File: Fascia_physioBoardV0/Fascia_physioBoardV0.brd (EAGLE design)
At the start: 32.8 x 41.6 mm, 81 parts, among them CN2 CA0612KRX7R9BB102, CN3 CA0612KRX7R9BB102, CN4 CA0612KRX7R9BB102, CN5 CA0612KRX7R9BB102, CN6 CA0612KRX7R9BB102, J1 MOLEX_52437-2471MOLEX_52437-2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, J2 MOLEX_52435-2271MOLEX_52435-2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, U1 ADS1299-X, U10 TPD4E1B06DCKR, U11 TPD4E1B06DCKR, U12 OPA320AIDBVRDBV5-L, U2 OPA2320AIDGKT_NOVA8-SOIC-L, U3 OPA2320AIDGKT_NOVAL8-SOIC-L, U4 HCNR200-300E, U5 OPA320AIDBVRDBV5-L, U6 TPD4E1B06DCKR, U7 TPD4E1B06DCKR, U8 TPD4E1B06DCKR, U9 TPD4E1B06DCKR

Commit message: minor updates
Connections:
- net ADS_CLK: now also J2.1
- net ADS_RESET2: now also J2.5
- net DVDD: now also J2.16, J2.17
- net DVDD_ISO: now also J2.20, J2.21
- net GND: now also J2.12, J2.13, J2.8, J2.9
- net GND_ISO: now also J2.18, J2.19
- net PA07_DRDY2: now also J2.2
- net PA16_S1_MOSI: now also J2.4
- net PA17_S1_SCK: now also J2.6
- net PA19_S1_MISO: now also J2.7
- net PA20_CS2: now also J2.3
- net S0_I2C_SCL: now also J2.11
- net S0_I2C_SDA: now also J2.10
- net VCC: now also J2.14, J2.15
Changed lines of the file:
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@@
 <drawing>
 <settings>
-<setting alwaysvectorfont="yes"/>
+<setting alwaysvectorfont="no"/>
 <setting verticaltext="up"/>
 </settings>
@@
 <signal name="PA19_S1_MISO">
 <contactref element="U1" pad="43"/>
+<contactref element="J2" pad="7"/>
+<wire x1="14.58" y1="29.838" x2="17.15" y2="37.138" width="0" layer="19" extent="1-1"/>
 </signal>
 <signal name="PA17_S1_SCK">
 <contactref element="U1" pad="40"/>
+<contactref element="J2" pad="6"/>
+<wire x1="16.08" y1="29.838" x2="17.65" y2="37.138" width="0" layer="19" extent="1-1"/>
 </signal>
 <signal name="N$66">
@@
 </polygon>
 <contactref element="U5" pad="5"/>
+<contactref element="J2" pad="16"/>
+<contactref element="J2" pad="17"/>
 <wire x1="18.58" y1="29.838" x2="24.05" y2="35.4332" width="0" layer="19" extent="1-16"/>
 <wire x1="12.08" y1="29.838" x2="18.58" y2="29.838" width="0" layer="19" extent="1-1"/>
@@
 <wire x1="8.342" y1="32.712" x2="12.08" y2="29.838" width="0" layer="19" extent="1-1"/>
 <wire x1="6.842" y1="32.712" x2="8.342" y2="32.712" width="0" layer="19" extent="1-1"/>
+<wire x1="12.15" y1="37.138" x2="8.342" y2="32.712" width="0" layer="19" extent="1-1"/>
+<wire x1="12.65" y1="37.138" x2="12.15" y2="37.138" width="0" layer="19" extent="1-1"/>
 </signal>
 <signal name="N$63">
@@
 <signal name="PA16_S1_MOSI">
 <contactref element="U1" pad="34"/>
+<contactref element="J2" pad="4"/>
+<wire x1="19.08" y1="29.838" x2="18.65" y2="37.138" width="0" layer="19" extent="1-1"/>
 </signal>
 <signal name="N$22">
@@
 <contactref element="U4" pad="5"/>
 <contactref element="U5" pad="3"/>
+<contactref element="J2" pad="8"/>
+<contactref element="J2" pad="9"/>
+<contactref element="J2" pad="12"/>
+<contactref element="J2" pad="13"/>
 <wire x1="25.95" y1="37.5668" x2="27.6" y2="37.8" width="0" layer="19" extent="16-16"/>
 <wire x1="25" y1="37.5668" x2="25.95" y2="37.5668" width="0" layer="19" extent="16-16"/>
 <wire x1="21.525" y1="41.01" x2="25" y2="37.5668" width="0" layer="19" extent="16-16"/>
-<wire x1="13.965" y1="40.3" x2="21.525" y2="41.01" width="0" layer="19" extent="1-16"/>
-<wire x1="16.008" y1="33.615" x2="21.525" y2="41.01" width="0" layer="19" extent="1-16"/>
+<wire x1="16.65" y1="37.138" x2="21.525" y2="41.01" width="0" layer="19" extent="1-16"/>
+<wire x1="16.15" y1="37.138" x2="16.65" y2="37.138" width="0" layer="19" extent="1-1"/>
+<wire x1="14.65" y1="37.138" x2="16.15" y2="37.138" width="0" layer="19" extent="1-1"/>
+<wire x1="14.15" y1="37.138" x2="14.65" y2="37.138" width="0" layer="19" extent="1-1"/>
+<wire x1="13.965" y1="40.3" x2="14.15" y2="37.138" width="0" layer="19" extent="1-1"/>
+<wire x1="16.008" y1="33.615" x2="16.15" y2="37.138" width="0" layer="19" extent="1-1"/>
 <wire x1="14.4515" y1="33.215" x2="16.008" y2="33.615" width="0" layer="19" extent="1-1"/>
 <wire x1="13.129" y1="33.215" x2="14.4515" y2="33.215" width="0" layer="19" extent="1-1"/>
@@
 <contactref element="U4" pad="4"/>
 <contactref element="U12" pad="2"/>
+<contactref element="J2" pad="18"/>
+<contactref element="J2" pad="19"/>
 <wire x1="27.191" y1="30.15" x2="25.85" y2="29.9" width="0" layer="19" extent="16-16"/>
-<wire x1="27.9" y1="23" x2="25.85" y2="29.9" width="0" layer="19" extent="16-16"/>
-<wire x1="25.65" y1="23" x2="27.9" y2="23" width="0" layer="19" extent="16-16"/>
+<wire x1="25.65" y1="23" x2="25.85" y2="29.9" width="0" layer="19" extent="16-16"/>
+<wire x1="27.9" y1="23" x2="25.65" y2="23" width="0" layer="19" extent="16-16"/>
 <wire x1="23.013" y1="23.495" x2="25.65" y2="23" width="0" layer="19" extent="16-16"/>
 <wire x1="16.05" y1="29.65" x2="23.013" y2="23.495" width="0" layer="19" extent="16-16"/>
@@
 <wire x1="5" y1="33.1332" x2="5.173" y2="30.831" width="0" layer="19" extent="16-16"/>
 <wire x1="4.05" y1="33.1332" x2="5" y2="33.1332" width="0" layer="19" extent="16-16"/>
+<wire x1="11.15" y1="37.138" x2="5" y2="33.1332" width="0" layer="19" extent="1-16"/>
+<wire x1="11.65" y1="37.138" x2="11.15" y2="37.138" width="0" layer="19" extent="1-1"/>
+<wire x1="10.275" y1="41.01" x2="11.15" y2="37.138" width="0" layer="19" extent="1-16"/>
 <wire x1="1.3" y1="21.1" x2="9.113" y2="23.195" width="0" layer="19" extent="16-16"/>
-<wire x1="10.275" y1="41.01" x2="5" y2="33.1332" width="0" layer="19" extent="16-16"/>
 </signal>
 <signal name="N$2">
@@
 <contactref element="U3" pad="8"/>
 <contactref element="U12" pad="5"/>
-<wire x1="25.65" y1="26.5" x2="24.258" y2="29.719" width="0" layer="19" extent="16-16"/>
-<wire x1="18.187" y1="27.305" x2="25.65" y2="26.5" width="0" layer="19" extent="16-16"/>
+<contactref element="J2" pad="20"/>
+<contactref element="J2" pad="21"/>
+<wire x1="24.258" y1="29.719" x2="25.65" y2="26.5" width="0" layer="19" extent="16-16"/>
+<wire x1="18.187" y1="27.305" x2="24.258" y2="29.719" width="0" layer="19" extent="16-16"/>
 <wire x1="10.275" y1="35.93" x2="18.187" y2="27.305" width="0" layer="19" extent="16-16"/>
+<wire x1="10.15" y1="37.138" x2="10.275" y2="35.93" width="0" layer="19" extent="1-16"/>
+<wire x1="10.65" y1="37.138" x2="10.15" y2="37.138" width="0" layer="19" extent="1-1"/>
 <wire x1="5.95" y1="35.2668" x2="10.275" y2="35.93" width="0" layer="19" extent="16-16"/>
 <wire x1="1.7" y1="33.4" x2="5.95" y2="35.2668" width="0" layer="19" extent="16-16"/>
@@
 <signal name="S0_I2C_SCL">
 <contactref element="J1" pad="22"/>
+<contactref element="J2" pad="11"/>
+<wire x1="20.4" y1="9.646" x2="15.15" y2="37.138" width="0" layer="19" extent="1-1"/>
 </signal>
 <signal name="PA20_CS2">
 <contactref element="U1" pad="39"/>
+<contactref element="J2" pad="3"/>
+<wire x1="16.58" y1="29.838" x2="19.15" y2="37.138" width="0" layer="19" extent="1-1"/>
 </signal>
 <signal name="N$12">
@@
 <signal name="S0_I2C_SDA">
 <contactref element="J1" pad="23"/>
+<contactref element="J2" pad="10"/>
+<wire x1="20.9" y1="9.646" x2="15.65" y2="37.138" width="0" layer="19" extent="1-1"/>
 </signal>
 <signal name="PA02_EDA_SIG">
@@
 <signal name="ADS_CLK">
 <contactref element="U1" pad="37"/>
+<contactref element="J2" pad="1"/>
+<wire x1="17.58" y1="29.838" x2="20.15" y2="37.138" width="0" layer="19" extent="1-1"/>
 </signal>
 <signal name="PA07_DRDY2">
 <contactref element="U1" pad="47"/>
+<contactref element="J2" pad="2"/>
+<wire x1="12.58" y1="29.838" x2="19.65" y2="37.138" width="0" layer="19" extent="1-1"/>
 </signal>
 <signal name="VCC">
 <contactref element="J1" pad="3"/>
 <contactref element="U11" pad="2"/>
-<wire x1="2.79" y1="14.16" x2="10.9" y2="9.646" width="0" layer="19" extent="1-1"/>
+<contactref element="J2" pad="14"/>
+<contactref element="J2" pad="15"/>
+<wire x1="13.15" y1="37.138" x2="13.65" y2="37.138" width="0" layer="19" extent="1-1"/>
+<wire x1="2.79" y1="14.16" x2="13.15" y2="37.138" width="0" layer="19" extent="1-1"/>
+<wire x1="10.9" y1="9.646" x2="2.79" y2="14.16" width="0" layer="19" extent="1-1"/>
 </signal>
 <signal name="ADS_RESET2">
 <contactref element="U1" pad="36"/>
+<contactref element="J2" pad="5"/>
+<wire x1="18.08" y1="29.838" x2="18.15" y2="37.138" width="0" layer="19" extent="1-1"/>
 </signal>
 <signal name="N$4">

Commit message: minor updates
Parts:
- removed SUPPLY1: 2PT_GND_TIE, SparkFun-PowerSymbols:2PT_GND_TIE
- added C41, C64: 10uF, SparkFun-Capacitors:0603
- added C49: 0.1uF, novaXR:0402-TIGHT
- added C51: 0.22uF, novaXR:0402-TIGHT
- added L1, L2: BLM15HD182SN1D, SamacSys_Parts:INDC1005X55N
- added U13: ADUM5028, novaXR:SOIC_IC
- J2: value MOLEX_52435-2271MOLEX_52435-2271_0_0 -> MOLEX_52437-2471MOLEX_52437-2471_0_0; device Molex - 52435-2271:MOLEX_52435-2271_0 -> Molex - 52437-2471:MOLEX_52437-2471_0
- moved R17 59.7 mm to (24.7, -25.6), turned to 270 degrees
- moved C16 58.7 mm to (23.7, -25.6), turned to 270 degrees
- moved C1 56.4 mm to (63.0, 27.3), turned to 0 degrees
- moved C25 55.6 mm to (20.4, -25.5), turned to 180 degrees
- moved C2 55.0 mm to (63.0, 26.3), turned to 0 degrees
- moved FD3 54.7 mm to (36.9, -5.10), turned to 90 degrees
- moved C27 53.5 mm to (19.8, -24.1), turned to 180 degrees
- moved C11 53.2 mm to (56.5, 27.1)
- moved C5 52.7 mm to (57.6, 27.1)
- moved C6 52.2 mm to (58.5, 27.1)
- moved C24 52.0 mm to (19.9, -22.6), turned to 0 degrees
- moved C26 51.6 mm to (14.2, -26.2), turned to 0 degrees
- moved C12 51.3 mm to (55.6, 27.1)
- moved R8 50.7 mm to (16.7, -23.9), turned to 0 degrees
- moved R7 48.8 mm to (14.2, -23.9), turned to 0 degrees
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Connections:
- new net N$6: C51.2, L1.1, U13.6
- net AGND: now also J2.17, J2.18; no longer SUPPLY1.P$1
- net AVDD: now also J2.21, J2.22
- net AVSS: now also J2.19, J2.20
- net BIAS_INV: now also J2.24
- net DVDD: now also C41.2, C49.2, J2.15, U13.3; no longer J2.17
- net DVDD_ISO: now also C64.2, L1.2; no longer J2.20, J2.21
- net GND: now also C41.1, C49.1, J2.10, J2.11, U13.1, U13.2, U13.4; no longer J2.13, J2.8, J2.9, SUPPLY1.P$2
- net GND_ISO: now also C51.1, C64.1, L2.1, L2.2, U13.5, U13.7, U13.8; no longer J2.18, J2.19
- net PA02_EDA_SIG: now also J2.23
- net S0_I2C_SCL: now also J2.9; no longer J2.11
- net S0_I2C_SDA: now also J2.8; no longer J2.10
- net VCC: now also J2.13; no longer J2.15
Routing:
- removed copper zone on layer 16, net AGND
- removed copper zone on layer 16, net GND
- removed copper zone on layer 16, net GND_ISO
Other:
- board size 32.8 x 41.6 mm -> 37.9 x 40 mm
- board text added: "When designing flex connector to board pay attention the flip that the board has to make in order to keep the WIFI module facing outward"

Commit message: minor updates
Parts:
- added J3: MOLEX_51296-1294MOLEX_51296-1294_0_0, Molex - 51296-1294:MOLEX_51296-1294_0
- moved RAW_EDA_SIG 22.2 mm to (41.0, -1.20)
- moved R4 9.70 mm to (27.2, 7.87)
- moved R3 9.14 mm to (27.5, 9.40)
- moved GND 8.23 mm to (37.8, 12.3)
- moved J1 6.26 mm to (12.8, 33.4)
- moved J2 3.91 mm to (33.9, 13.8)
- moved U11 3.01 mm to (34.0, 29.2)
- moved U6 2.41 mm to (28.4, 29.1)
- moved RN3 2.00 mm to (16.4, 26.1)
- moved CN4 1.90 mm to (16.5, 23.0)
- moved U12 1.65 mm to (21.8, 17.4)
- moved U7 1.60 mm to (22.6, 28.8)
- moved U5 1.60 mm to (30.9, 17.3)
- moved U13 1.32 mm to (6.00, 11.1)
- moved U4 1.30 mm to (26.4, 8.20)
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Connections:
- net 1N: now also J1.14; no longer J1.20
- net 1P: now also J1.15; no longer J1.21
- net 2N: now also J1.12; no longer J1.18
- net 2P: now also J1.13; no longer J1.19
- net 3N: now also J1.10; no longer J1.16
- net 3P: now also J1.11; no longer J1.17
- net 4N: now also J1.8; no longer J1.14
- net 4P: now also J1.9; no longer J1.15
- net 5N: now also J1.6; no longer J1.12
- net 5P: now also J1.7; no longer J1.13
- net 6N: now also J1.4; no longer J1.10
- net 6P: now also J1.5; no longer J1.11
- net 7N: now also J3.3; no longer J1.8
- net 7P: no longer J1.9
- net 8N: now also J3.9; no longer J1.6
- net 8P: no longer J1.7
- net AGND: now also J1.16, J1.17, J1.18, J3.10, J3.4; no longer J1.24
- net AVDD: now also J3.11, J3.12, J3.5, J3.6
- net AVSS: now also J3.1, J3.2, J3.7, J3.8
- net BIAS: now also J1.3; no longer J1.5
- net GND: now also J1.19, J1.20; no longer J1.4
- net S0_I2C_SCL: now also J1.23; no longer J1.22
- net S0_I2C_SDA: now also J1.24; no longer J1.23
- net VCC: now also J1.21, J1.22; no longer J1.3
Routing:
- net IN8P: track 0.00 -> 17.2 mm
- net IN8N: track 0.00 -> 16.3 mm
- net IN7N: track 0.00 -> 14.5 mm
- net IN7P: track 0.00 -> 14.4 mm
- net IN6N: track 0.00 -> 14.3 mm
- net IN6P: track 0.00 -> 14.3 mm
- net IN1P: track 0.00 -> 13.5 mm
- net IN1N: track 0.00 -> 13.0 mm
- net IN2P: track 0.00 -> 11.5 mm
- net IN2N: track 0.00 -> 11.0 mm
- net IN3P: track 0.00 -> 10.6 mm
- net IN3N: track 0.00 -> 10.3 mm
- net IN4P: track 0.00 -> 10.1 mm
- net IN4N: track 0.00 -> 9.84 mm
- net IN5P: track 0.00 -> 9.65 mm
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- removed copper zone on layer 15, net AGND
- removed copper zone on layer 2, net AVDD
- removed copper zone on layer 2, net AVSS
- removed copper zone on layer 2, net DVDD
- removed copper zone on layer 1, net GND
- removed copper zone on layer 15, net GND

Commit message: minor changes
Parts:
- R7: value 39K -> 20K
- R8: value 150K -> 140K
- R9: value 2M -> 875K
- moved C6 42.0 mm to (23.8, 3.50)
- moved C5 40.3 mm to (24.9, 3.50)
- moved FD4 39.6 mm to (11.6, 34.6)
- moved C1 34.7 mm to (29.5, 18.4)
- moved C2 34.7 mm to (29.5, 17.4)
- moved C11 32.1 mm to (25.9, 17.3), turned to 225 degrees
- moved C12 31.7 mm to (25.3, 18.0), turned to 225 degrees
- moved C9 28.9 mm to (23.6, 19.7), turned to 45 degrees
- moved R2 28.5 mm to (22.8, 20.5), turned to 45 degrees
- moved C49 26.3 mm to (6.60, 3.50)
- moved C51 23.2 mm to (6.50, 16.1)
- moved C41 23.0 mm to (6.50, 2.00)
- moved L2 21.8 mm to (7.00, 17.9)
- moved L1 21.8 mm to (5.70, 18.0)
- moved C64 21.3 mm to (6.40, 20.0)
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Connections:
- net 7N: now also J3.9; no longer J3.3
- net 8N: now also J3.3; no longer J3.9
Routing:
- net _SRB2: track 5.78 -> 20.0 mm
- net _SRB1: track 5.12 -> 16.7 mm
- net IN7N: track 14.5 -> 12.0 mm
- net IN7P: track 14.4 -> 11.9 mm
- net IN6N: track 14.3 -> 12.1 mm
- net IN6P: track 14.3 -> 12.1 mm

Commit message: minor updates
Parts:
- moved FD5 52.9 mm to (5.25, 35.0)
- moved C16 47.6 mm to (35.0, 20.6), turned to 0 degrees
- moved R17 46.3 mm to (34.9, 19.6), turned to 0 degrees
- moved C25 44.8 mm to (18.2, 19.2), turned to 90 degrees
- moved C27 42.9 mm to (16.9, 18.6), turned to 90 degrees
- moved C26 40.4 mm to (19.4, 13.9), turned to 270 degrees
- moved R8 39.6 mm to (16.6, 15.6), turned to 270 degrees
- moved R7 38.4 mm to (17.9, 14.3), turned to 270 degrees
- moved RAW_EDA_SIG 37.4 mm to (5.30, 10.0)
- moved R9 35.8 mm to (17.1, 20.9), turned to 0 degrees
- moved C24 35.4 mm to (15.2, 12.5)
- moved FD1 29.5 mm to (34.8, 34.6)
- moved C10 25.5 mm to (25.9, 19.7), turned to 180 degrees
- moved R11 24.0 mm to (11.8, 10.8)
- moved C28 23.9 mm to (11.7, 11.6), turned to 180 degrees
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
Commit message: minor layout changes
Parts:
- moved C6 15.7 mm to (23.8, 19.2), turned to 225 degrees
- moved C5 15.1 mm to (24.5, 18.6), turned to 45 degrees
- moved R16 14.9 mm to (28.5, 15.9), turned to 180 degrees
- moved C20 13.5 mm to (15.6, 5.03), turned to 225 degrees
- moved DVDD_ISO 11.0 mm to (27.8, 18.3)
- moved RAW_EDA_SIG 9.04 mm to (10.5, 2.60)
- moved R6 8.91 mm to (25.4, 7.15), turned to 135 degrees
- moved R1 8.87 mm to (24.4, 6.16), turned to 135 degrees
- moved GND_ISO 8.41 mm to (19.1, 20.8)
- moved C1 8.04 mm to (28.1, 10.4), turned to 135 degrees
- moved C2 6.24 mm to (28.7, 11.2), turned to 135 degrees
- moved PA02_EDA_SIG 5.66 mm to (34.5, 21.7)
- moved C30 4.95 mm to (18.8, 7.55)
- moved C3 4.30 mm to (8.25, 9.53)
- moved C4 4.13 mm to (7.40, 9.53)
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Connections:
- net AVDD: now also U11.2
- net VCC: no longer U11.2
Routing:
- net GND: track 0.00 -> 13.2 mm, vias 0 -> 9
- net BIAS_DRV: track 0.00 -> 12.3 mm
- net N$17: track 0.00 -> 4.30 mm
- net N$63: track 0.00 -> 2.73 mm
- net AGND: track 0.00 -> 0.59 mm, vias 0 -> 1
- added copper zone on layer 2, net AGND
- added copper zone on layer 2, net GND
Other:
- board size 37.9 x 40 mm -> 37.3 x 39.1 mm

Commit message: wiring progress
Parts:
- moved C13 11.7 mm to (29.6, 19.3)
- moved C14 11.6 mm to (29.6, 18.2)
- moved FD2 9.95 mm to (34.8, 25.4)
- moved C3 4.41 mm to (5.15, 12.7)
- moved C4 3.44 mm to (6.00, 12.7)
- moved U11 2.80 mm to (31.4, 28.6)
- moved C29 2.02 mm to (18.2, 6.00), turned to 180 degrees
- moved FD6 1.91 mm to (4.65, 6.10)
- moved L2 1.90 mm to (5.10, 18.3)
- moved R13 1.72 mm to (18.2, 4.10), turned to 180 degrees
- moved U6 1.50 mm to (26.3, 28.7)
- moved U7 1.40 mm to (21.2, 28.8)
- moved C49 1.30 mm to (5.60, 4.50), turned to 180 degrees
- moved C41 1.30 mm to (5.60, 2.50), turned to 180 degrees
- moved C7 1.03 mm to (16.2, 4.39), turned to 225 degrees
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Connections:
- removed net PA07_DRDY2: J2.2, U1.47
- new net PA07_DRDY: J2.7, U1.47
- net ADS_CLK: now also J2.3; no longer J2.1
- net ADS_RESET2: now also J2.2; no longer J2.5
- net PA16_S1_MOSI: now also J2.1; no longer J2.4
- net PA17_S1_SCK: now also J2.5; no longer J2.6
- net PA19_S1_MISO: now also J2.6; no longer J2.7
- net PA20_CS2: now also J2.4; no longer J2.3
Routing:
- net GND: track 13.2 -> 86.6 mm, vias 9 -> 12
- net S0_I2C_SDA: track 0.00 -> 67.9 mm
- net S0_I2C_SCL: track 0.00 -> 65.5 mm
- net VCC: track 0.00 -> 60.6 mm
- net AVSS: track 0.00 -> 47.7 mm, vias 0 -> 9
- net N$7: track 0.00 -> 18.0 mm
- net N$3: track 0.00 -> 17.3 mm
- net PA16_S1_MOSI: track 0.00 -> 17.2 mm
- net DVDD: track 0.00 -> 16.9 mm, vias 0 -> 5
- net ADS_RESET2: track 0.00 -> 16.4 mm
- net ADS_CLK: track 0.00 -> 16.1 mm
- net BIAS_INV: track 0.00 -> 13.9 mm
- net PA20_CS2: track 0.00 -> 13.8 mm
- net PA17_S1_SCK: track 0.00 -> 13.5 mm
- net AVDD: track 0.00 -> 13.2 mm, vias 0 -> 5
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- added copper zone on layer 15, net AVDD
- added copper zone on layer 15, net AVSS
- added copper zone on layer 15, net DVDD

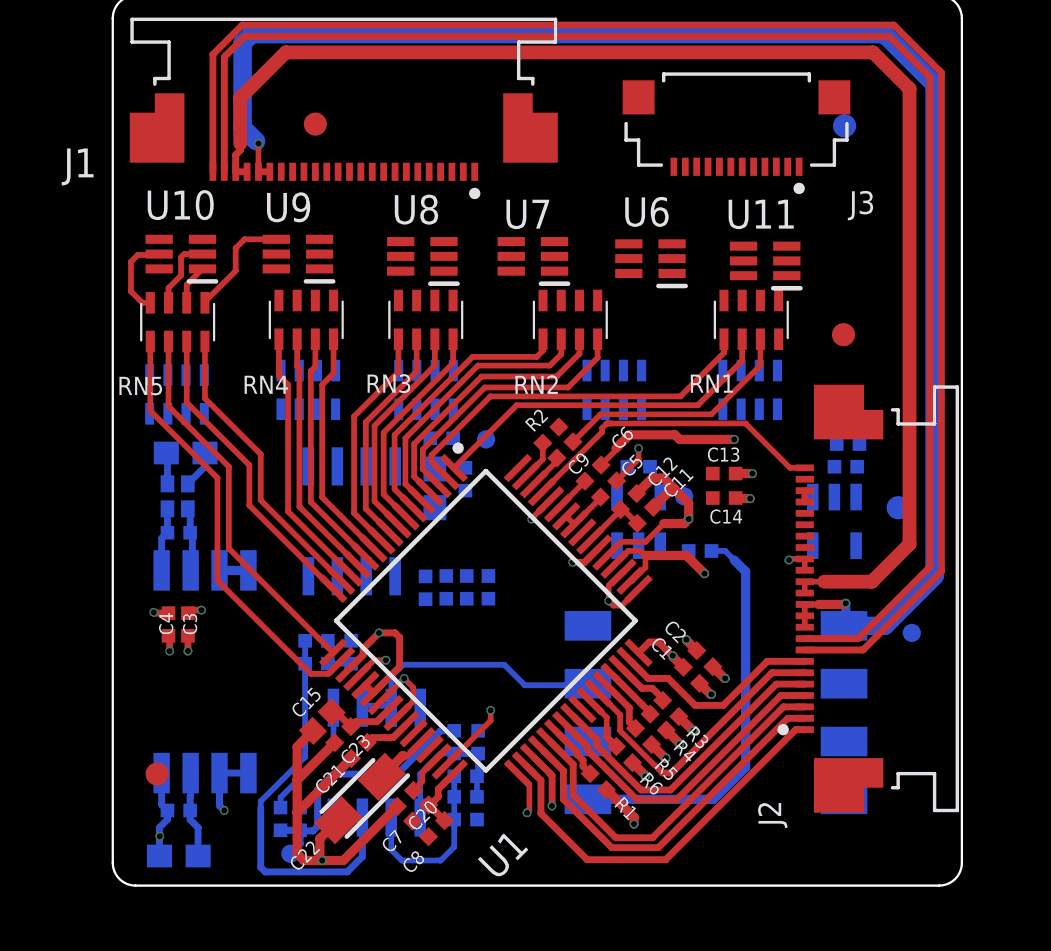
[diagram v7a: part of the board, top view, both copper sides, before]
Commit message: finished routing physio board, bunch of warnings in ERC and a few width errors in DRC
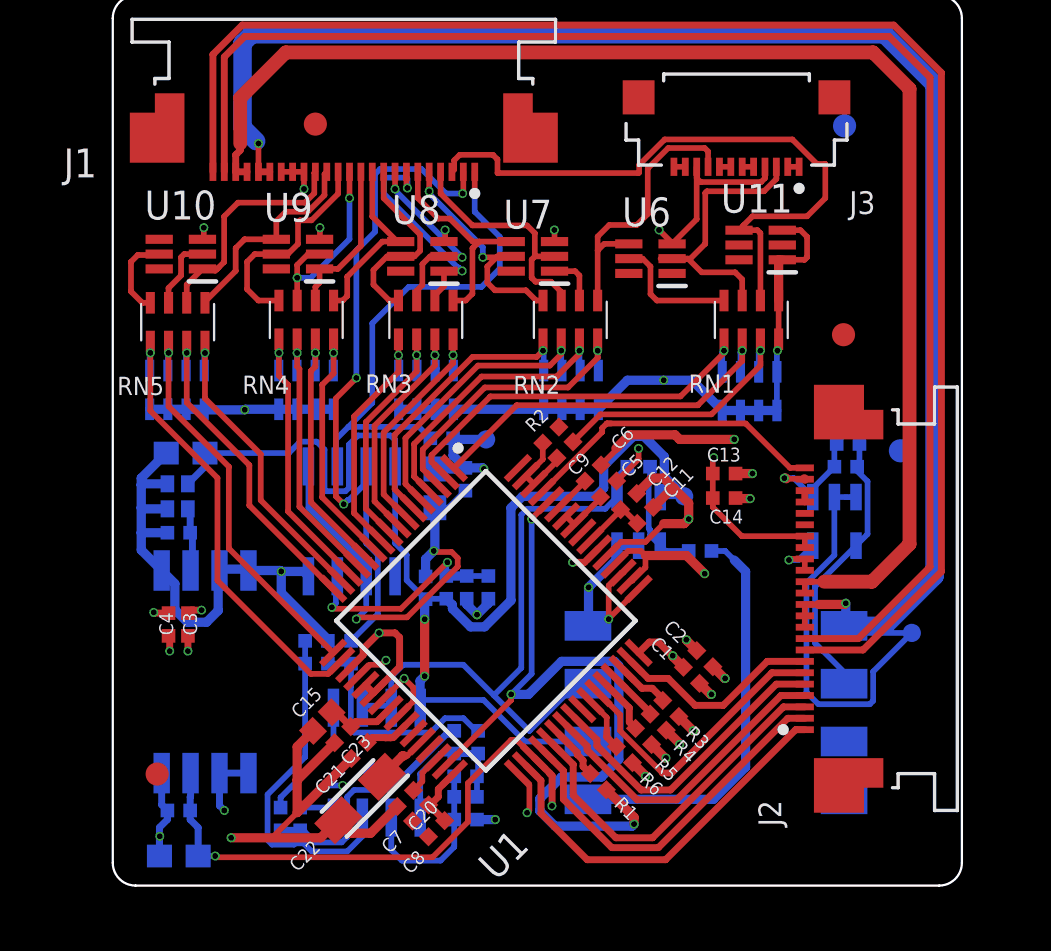
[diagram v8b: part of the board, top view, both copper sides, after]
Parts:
- moved RAW_EDA_SIG 5.09 mm to (14.1, 6.20)
- moved FD3 2.50 mm to (37.3, 20.3)
- moved CN3 1.90 mm to (22.8, 23.0)
- moved U11 0.73 mm to (31.2, 29.3)
- moved CN6 0.20 mm to (5.52, 23.0)
- moved CN5 0.10 mm to (11.2, 23.0)
- moved CN2 0.06 mm to (30.7, 22.9)
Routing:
- net AGND: track 6.42 -> 90.1 mm, vias 3 -> 13
- net DVDD_ISO: track 1.66 -> 56.3 mm, vias 0 -> 2
- net GND_ISO: track 5.45 -> 40.6 mm, vias 0 -> 6
- net EDA-: track 0.00 -> 31.2 mm, vias 0 -> 3
- net BIAS: track 0.00 -> 28.7 mm
- net EDA+: track 0.00 -> 22.1 mm, vias 0 -> 1
- net GND: track 86.6 -> 107.6 mm
- net DVDD: track 16.9 -> 36.4 mm, vias 5 -> 6
- net N$12: track 0.00 -> 19.4 mm, vias 0 -> 2
- net N$15: track 11.9 -> 28.1 mm
- net 8N: track 0.00 -> 12.8 mm
- net 7N: track 0.00 -> 12.7 mm
- net N$9: track 0.00 -> 12.2 mm
- net 6N: track 0.00 -> 10.6 mm
- net 6P: track 0.00 -> 10.1 mm, vias 0 -> 2
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- added copper zone on layer 2, net GND_ISO
